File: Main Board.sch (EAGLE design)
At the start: 55 parts, among them IC1 ATSAMD21G18A-AF, IC2 BMP388, IC3 CAT24C64WI-GT3, IC4 DRV2605, IC6 MIC5219-3.3YM5, IC7 MIC5219-5.0YM5, J1 10118194-0001LF, Q1 BC817-25LT1SMD, Y1 ECS-.327-7-34B-TR

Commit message: 6 pin SH connector instead of two 4 pin SH connectors
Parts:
- removed ESC, TELEM: BM04B-SRSS-TB(LF)(SN), Braedin's Eagle Libraries:BM04B-SRSS-TB(LF)(SN)
- added J2: BM06B-SRSS-TB(LF)(SN), BM06B-SRSS-TB(LF)(SN):BM06B-SRSS-TB(LF)(SN)
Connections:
- net 12V: now also J2.1; no longer TELEM.P$1
- net 5V: now also J2.5; no longer ESC.P$3
- net D12_TO_ESC: now also J2.6; no longer ESC.P$4
- net GND: now also J2.4; no longer ESC.P$2, TELEM.P$4
- net RX0_FROM_ESC: now also J2.2; no longer TELEM.P$2
- net TX1_TO_ESC: now also J2.3; no longer TELEM.P$3
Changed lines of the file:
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@@
 <part name="R8" library="rcl" library_urn="urn:adsk.eagle:library:334" deviceset="R-US_" device="R0402" value="4.7k"/>
 <part name="R11" library="rcl" library_urn="urn:adsk.eagle:library:334" deviceset="R-US_" device="R0402" value="4.7k"/>
-<part name="ESC" library="Braedin's Eagle Libraries" deviceset="BM04B-SRSS-TB(LF)(SN)" device="" value="BM04B-SRSS-TB(LF)(SN)"/>
-<part name="TELEM" library="Braedin's Eagle Libraries" deviceset="BM04B-SRSS-TB(LF)(SN)" device="" value="BM04B-SRSS-TB(LF)(SN)"/>
-<part name="SUPPLY30" library="supply2" library_urn="urn:adsk.eagle:library:372" deviceset="GND" device=""/>
-<part name="SUPPLY32" library="supply2" library_urn="urn:adsk.eagle:library:372" deviceset="GND" device=""/>
+<part name="J2" library="BM06B-SRSS-TB(LF)(SN)" deviceset="BM06B-SRSS-TB(LF)(SN)" device=""/>
+<part name="SUPPLY6" library="supply2" library_urn="urn:adsk.eagle:library:372" deviceset="GND" device=""/>
 </parts>
 <sheets>
@@
 <attribute name="VALUE" x="635.762" y="262.89" size="1.778" layer="96" rot="R90"/>
 </instance>
-<instance part="ESC" gate="G$1" x="373.38" y="109.22" smashed="yes">
-<attribute name="NAME" x="363.22" y="124.46" size="1.778" layer="95"/>
-<attribute name="VALUE" x="363.22" y="93.98" size="1.778" layer="96"/>
-</instance>
-<instance part="TELEM" gate="G$1" x="373.38" y="58.42" smashed="yes">
-<attribute name="NAME" x="363.22" y="73.66" size="1.778" layer="95"/>
-<attribute name="VALUE" x="363.22" y="43.18" size="1.778" layer="96"/>
-</instance>
-<instance part="SUPPLY30" gate="GND" x="342.9" y="109.22" smashed="yes">
-<attribute name="VALUE" x="340.995" y="106.045" size="1.778" layer="96"/>
-</instance>
-<instance part="SUPPLY32" gate="GND" x="342.9" y="48.26" smashed="yes">
-<attribute name="VALUE" x="340.995" y="45.085" size="1.778" layer="96"/>
+<instance part="J2" gate="G$1" x="353.06" y="111.76" smashed="yes">
+<attribute name="NAME" x="369.57" y="119.38" size="1.778" layer="95" align="center-left"/>
+<attribute name="VALUE" x="369.57" y="116.84" size="1.778" layer="96" align="center-left"/>
+</instance>
+<instance part="SUPPLY6" gate="GND" x="322.58" y="106.68" smashed="yes">
+<attribute name="VALUE" x="320.675" y="103.505" size="1.778" layer="96"/>
 </instance>
 </instances>
@@
 </segment>
 <segment>
-<pinref part="ESC" gate="G$1" pin="P$2"/>
-<wire x1="360.68" y1="111.76" x2="342.9" y2="111.76" width="0.1524" layer="91"/>
-<pinref part="SUPPLY30" gate="GND" pin="GND"/>
-</segment>
-<segment>
-<pinref part="TELEM" gate="G$1" pin="P$4"/>
-<wire x1="360.68" y1="50.8" x2="342.9" y2="50.8" width="0.1524" layer="91"/>
-<pinref part="SUPPLY32" gate="GND" pin="GND"/>
+<pinref part="J2" gate="G$1" pin="4"/>
+<wire x1="353.06" y1="109.22" x2="322.58" y2="109.22" width="0.1524" layer="91"/>
+<pinref part="SUPPLY6" gate="GND" pin="GND"/>
 </segment>
 </net>
@@
 </segment>
 <segment>
-<pinref part="ESC" gate="G$1" pin="P$3"/>
-<wire x1="360.68" y1="106.68" x2="358.14" y2="106.68" width="0.1524" layer="91"/>
-<label x="358.14" y="106.68" size="1.778" layer="95" rot="R180" xref="yes"/>
+<pinref part="J2" gate="G$1" pin="5"/>
+<wire x1="373.38" y1="111.76" x2="375.92" y2="111.76" width="0.1524" layer="91"/>
+<label x="375.92" y="111.76" size="1.778" layer="95" xref="yes"/>
 </segment>
 </net>
@@
 </segment>
 <segment>
-<pinref part="ESC" gate="G$1" pin="P$4"/>
-<wire x1="360.68" y1="101.6" x2="358.14" y2="101.6" width="0.1524" layer="91"/>
-<label x="358.14" y="101.6" size="1.778" layer="95" rot="R180" xref="yes"/>
+<pinref part="J2" gate="G$1" pin="6"/>
+<wire x1="353.06" y1="111.76" x2="350.52" y2="111.76" width="0.1524" layer="91"/>
+<label x="350.52" y="111.76" size="1.778" layer="95" rot="R180" xref="yes"/>
 </segment>
 </net>
@@
 </segment>
 <segment>
-<pinref part="TELEM" gate="G$1" pin="P$2"/>
-<wire x1="360.68" y1="60.96" x2="358.14" y2="60.96" width="0.1524" layer="91"/>
-<label x="358.14" y="60.96" size="1.778" layer="95" rot="R180" xref="yes"/>
+<pinref part="J2" gate="G$1" pin="2"/>
+<wire x1="353.06" y1="106.68" x2="350.52" y2="106.68" width="0.1524" layer="91"/>
+<label x="350.52" y="106.68" size="1.778" layer="95" rot="R180" xref="yes"/>
 </segment>
 </net>
@@
 </segment>
 <segment>
-<pinref part="TELEM" gate="G$1" pin="P$1"/>
-<wire x1="360.68" y1="66.04" x2="358.14" y2="66.04" width="0.1524" layer="91"/>
-<label x="358.14" y="66.04" size="1.778" layer="95" rot="R180" xref="yes"/>
+<pinref part="J2" gate="G$1" pin="1"/>
+<wire x1="373.38" y1="106.68" x2="375.92" y2="106.68" width="0.1524" layer="91"/>
+<label x="375.92" y="106.68" size="1.778" layer="95" xref="yes"/>
 </segment>
 </net>
@@
 </segment>
 <segment>
-<pinref part="TELEM" gate="G$1" pin="P$3"/>
-<wire x1="360.68" y1="55.88" x2="358.14" y2="55.88" width="0.1524" layer="91"/>
-<label x="358.14" y="55.88" size="1.778" layer="95" rot="R180" xref="yes"/>
-</segment>
-</net>
+<pinref part="J2" gate="G$1" pin="3"/>
+<wire x1="373.38" y1="109.22" x2="375.92" y2="109.22" width="0.1524" layer="91"/>
+<label x="375.92" y="109.22" size="1.778" layer="95" xref="yes"/>
+</segment>
+</net>

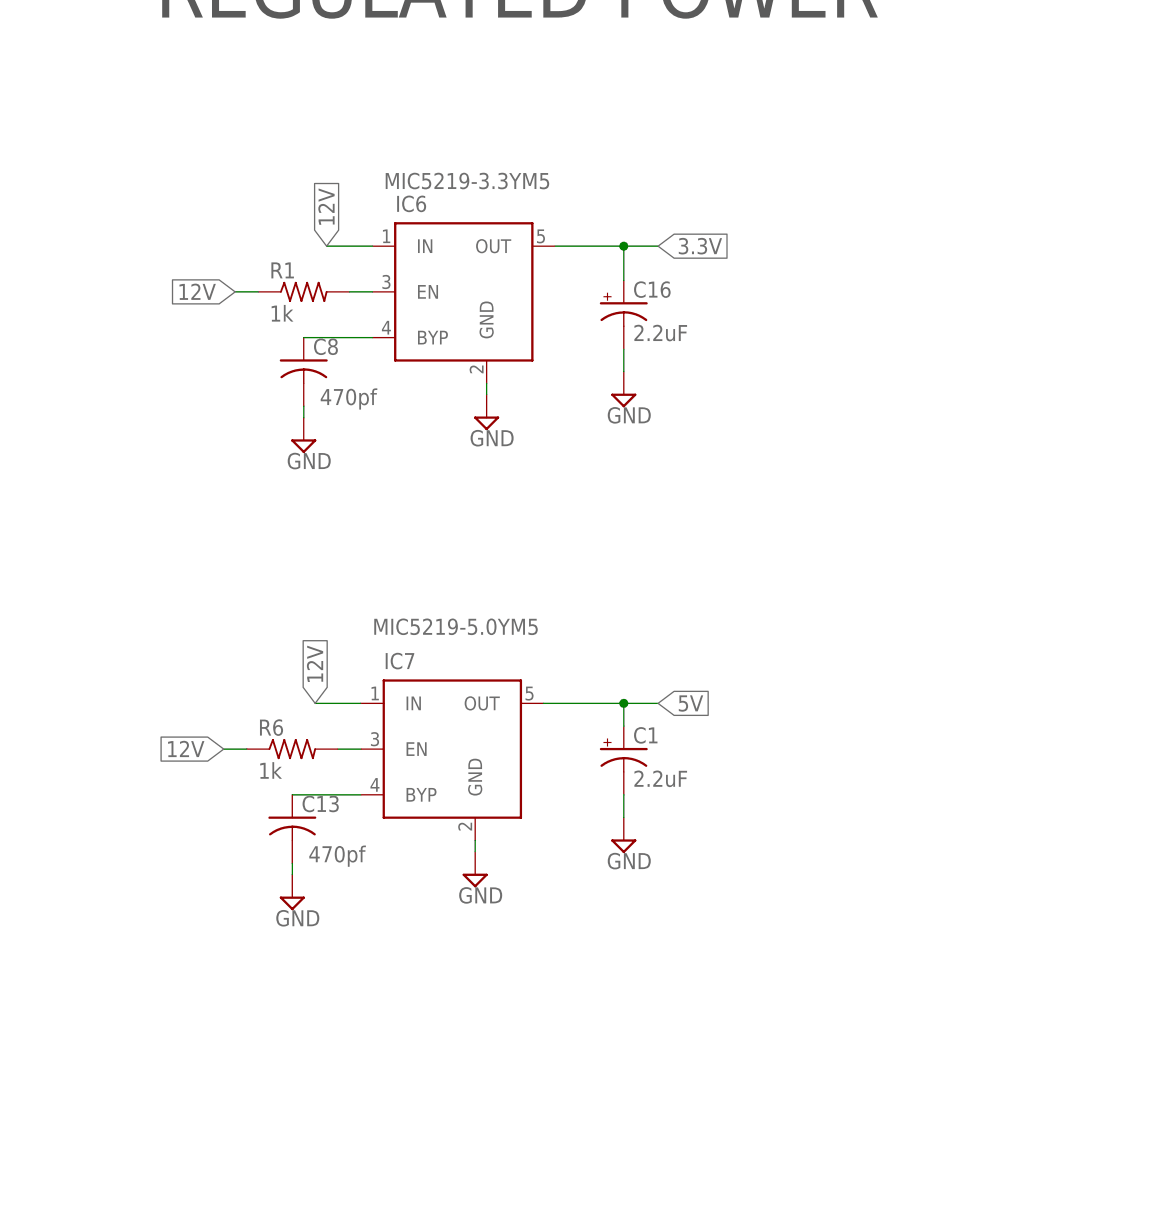
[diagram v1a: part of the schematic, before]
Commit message: Switching regulator to reduce heat, and added ground planes
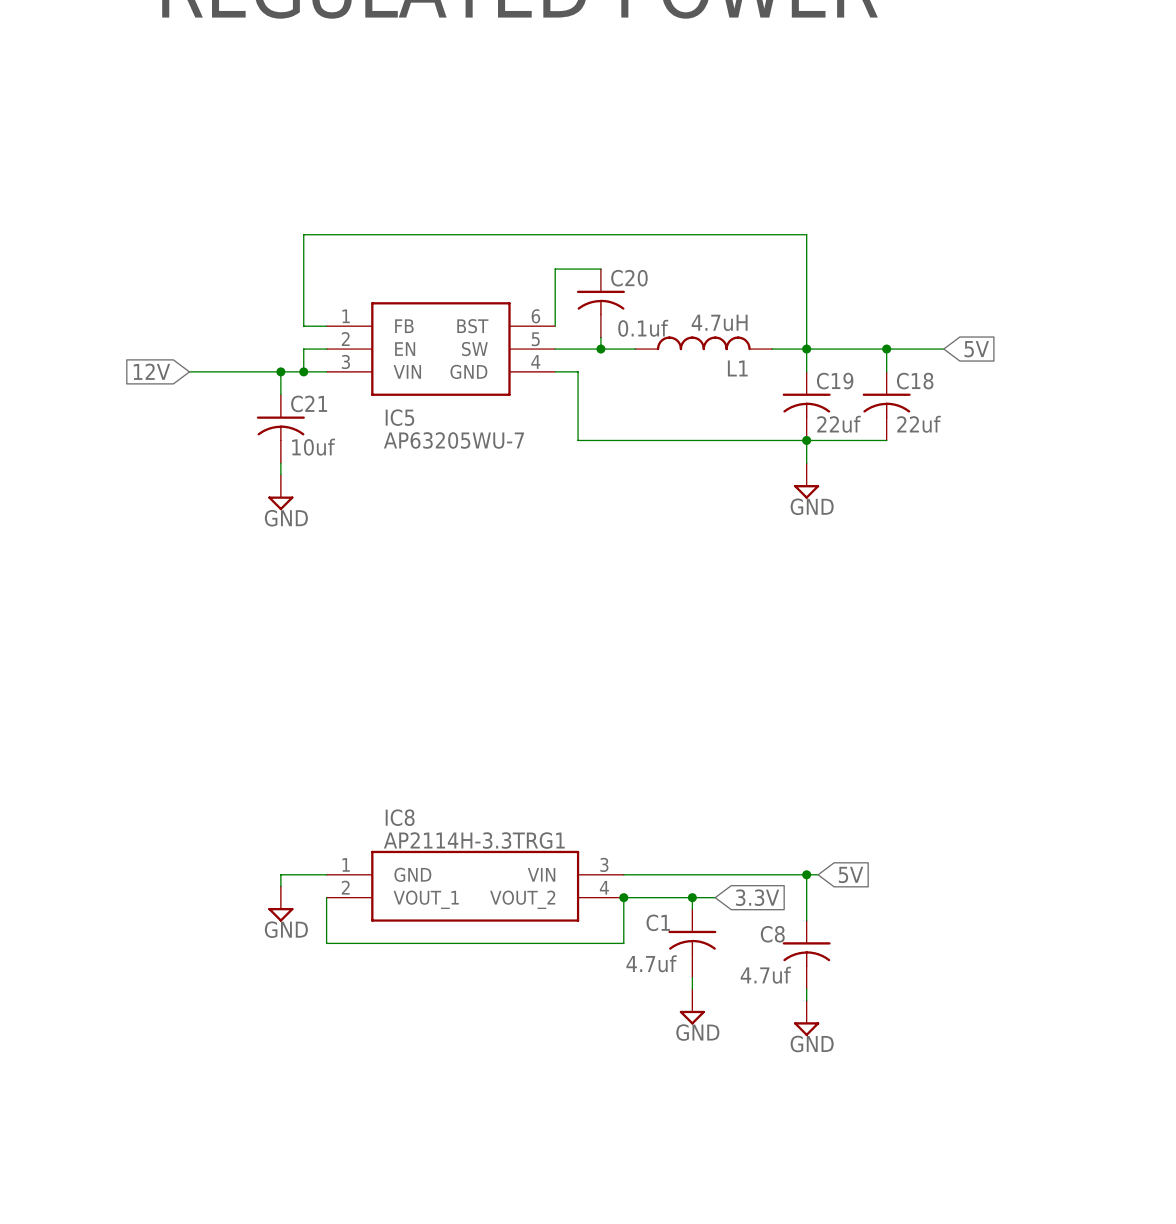
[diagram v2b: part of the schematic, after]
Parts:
- removed C13: 470pf, rcl:C-USC0402
- removed C16: 2.2uF, adafruit:CPOL-USCT3216
- removed IC6: MIC5219-3.3YM5, v-reg-micrel:MIC5219XX
- removed IC7: MIC5219-5.0YM5, v-reg-micrel:MIC5219XX
- removed R1, R6: 1k, rcl:R-US_R0402
- added C18, C19: 22uf, rcl:C-USC0603
- added C20: 0.1uf, rcl:C-USC0402
- added C21: 10uf, rcl:C-USC0805
- added IC5: AP63205WU-7, AP63205WU-7:AP63205WU-7
- added IC8: AP2114H-3.3TRG1, AP2114H-3.3TRG1:AP2114H-3.3TRG1
- added L1: 4.7uH, rcl:L-USL1812
- C1: value 2.2uF -> 4.7uf; device adafruit:CPOL-USCT3216 -> rcl:C-USC0402
- C8: value 470pf -> 4.7uf
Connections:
- removed net N$12: C8.1, IC6.BYP
- removed net N$3: IC6.EN, R1.2
- removed net N$5: IC7.EN, R6.2
- removed net N$7: C13.1, IC7.BYP
- new net N$10: C20.2, IC5.SW, L1.1
- new net N$11: C20.1, IC5.BST
- net 12V: now also C21.1, IC5.EN, IC5.VIN; no longer IC6.IN, IC7.IN, R1.1, R6.1
- net 3.3V: now also C1.1, IC8.VOUT_1, IC8.VOUT_2; no longer C16.+, IC6.OUT
- net 5V: now also C18.1, C19.1, C8.1, IC5.FB, IC8.VIN, L1.2; no longer C1.+, IC7.OUT
- net GND: now also C1.2, C18.2, C19.2, C21.2, IC5.GND, IC8.GND; no longer C1.-, C13.2, C16.-, IC6.GND, IC7.GND
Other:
- moved on the sheet: C8

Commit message: Rx and Tx to pin 37 and 38; Shifted location of JST; Added holes for zip tie
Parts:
- added R1: 1k, rcl:R-US_R0402
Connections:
- net GND: now also R1.2
- net RX0_FROM_ESC: now also IC1.PB23, R1.1; no longer IC1.PA11
- net TX1_TO_ESC: no longer IC1.PA10
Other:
- moved on the sheet: LED1, R3
